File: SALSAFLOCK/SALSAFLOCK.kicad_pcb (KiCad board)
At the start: 2 copper layers, 30.8 x 52.8 mm, 15 parts, among them J1 DB15-VGA, J2 DB15-VGA, P2 ANTENNA, Q1 MOSFET_N, Q2 MOSFET_N

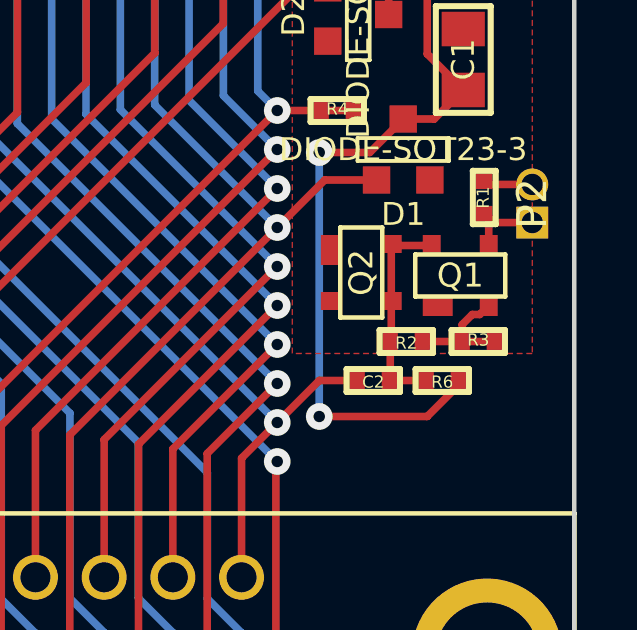
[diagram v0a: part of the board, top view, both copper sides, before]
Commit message: connected BSS83,215 substrate to source (previous workaround was solder blob)
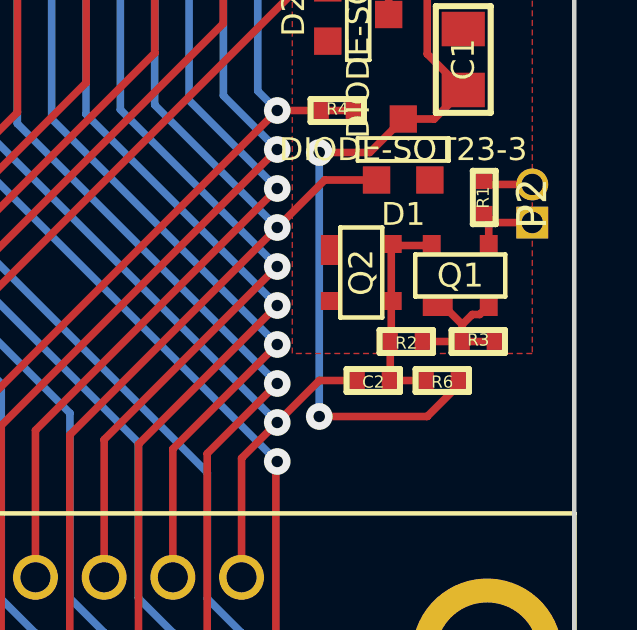
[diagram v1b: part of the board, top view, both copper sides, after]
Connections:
- Q1 pad B: (no net) -> /SOURCE
- Q2 pad B: (no net) -> GND
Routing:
- net /SOURCE: track 3.05 -> 4.12 mm

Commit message: changed R6 to 10k
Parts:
- R6: value 1M -> 10k
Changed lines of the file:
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@@
       (effects (font (size 0.4064 0.4064) (thickness 0.1016)))
     )
-    (fp_text value 1M (at 0 0.0508) (layer F.SilkS) hide
+    (fp_text value 10k (at 0 0.0508) (layer F.SilkS) hide
       (effects (font (size 0.4064 0.4064) (thickness 0.1016)))
     )
@@
   (segment (start 119 100) (end 131 88) (width 0.254) (layer F.Cu) (net 5))
   (via (at 119 100) (size 0.889) (layers F.Cu B.Cu) (net 5))
-  (segment (start 135.85 98.4) (end 136.0332 98.4) (width 0.254) (layer F.Cu) (net 7) (status C00000))
-  (segment (start 136.0332 98.4) (end 136.6666 99.0334) (width 0.254) (layer F.Cu) (net 7) (status 400000))
+  (segment (start 135.85 98.4) (end 136.0332 98.4) (width 0.254) (layer F.Cu) (net 7))
+  (segment (start 136.0332 98.4) (end 136.6666 99.0334) (width 0.254) (layer F.Cu) (net 7))
   (segment (start 136.6666 99.6) (end 136.6666 99.0334) (width 0.254) (layer F.Cu) (net 7))
   (segment (start 137.25 98.7) (end 137.55 98.4) (width 0.254) (layer F.Cu) (net 7))
